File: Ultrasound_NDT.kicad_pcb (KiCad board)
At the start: 6 copper layers, 100 x 100 mm, 316 parts, among them J1 Conn_01x02_Pin, J10 CONSMA002-SMD, J11 Logger Connector, J12 UART Connector, J13 External UART, J14 External I2C, J15 JTAG Header, J16 Conn_02x04_Odd_Even, J17 Input Power, J18 Conn_01x02_Pin, J19 Conn_01x02_Pin, J2 Conn_01x02_Pin, J20 Conn_01x02_Pin, J21 Conn_01x02_Pin, J22 Conn_01x02_Pin, J23 Conn_01x02_Pin, J24 Conn_01x02_Pin, J25 Conn_01x02_Pin, J26 Spectrography Power, J27 Conn_01x02_Pin, J28 Conn_02x04_Odd_Even, J3 CONSMA002-SMD, J4 CONSMA002-SMD, J5 CONSMA002-SMD, J6 CONSMA002-SMD, J7 CONSMA002-SMD, J8 CONSMA002-SMD, J9 CONSMA002-SMD, SW1 XRSn_button, U1 AD8334ACPZ, U10 TLV9354IDR, U11 TLV9354IDR, U12 TPS63700DRCR, U13 M24M01E-FMN6TP, U14 LDL212PU50R, U15 AZ1117CH2-3.3, U16 AZ1117CH2-3.3, U17 TRS3221EIPWR, U2 DSC1001DI2-125.0000T, U3 MAX14808ETK_, U4 AD8334ACPZ, U5 F280025PNS, U6 REF3030, U7 MIC920YC5-TR, U8 TLV9354IDR, U9 TLV9354IDR, Y2 H130B-16.000-18-3030-EXT-TR

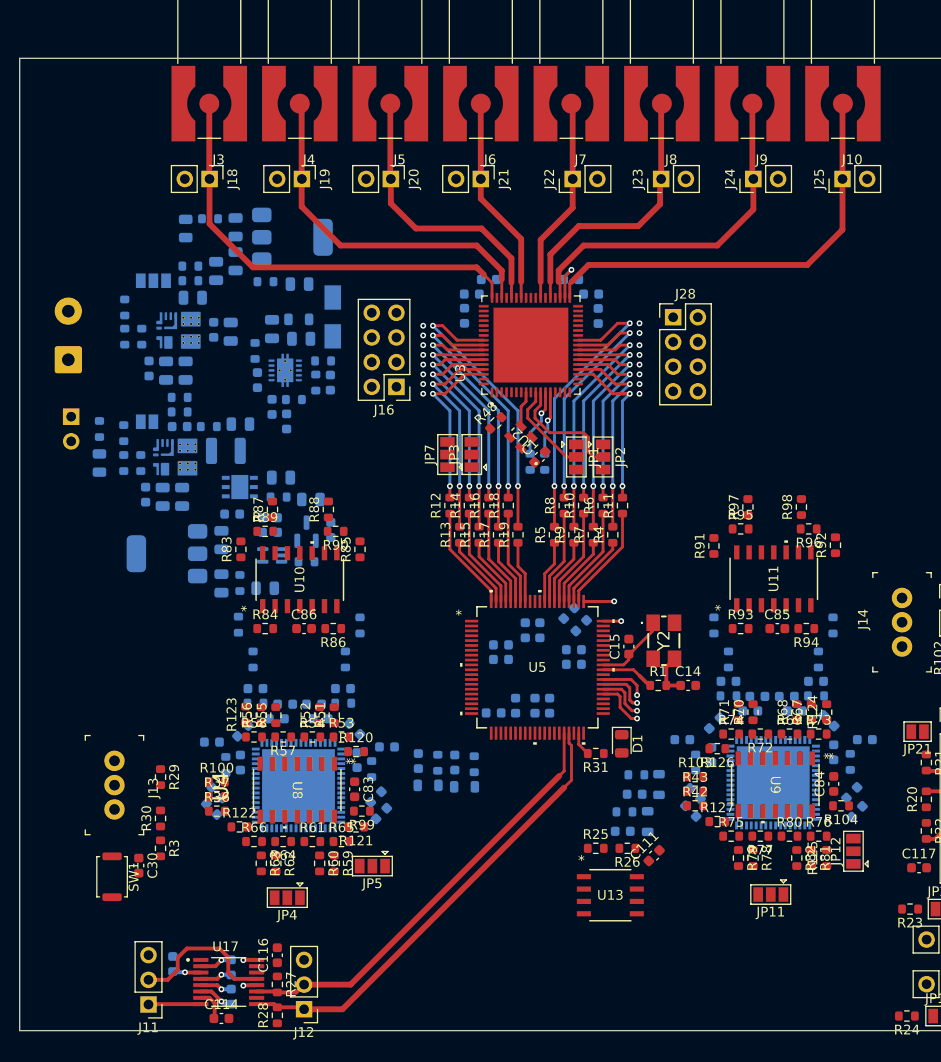
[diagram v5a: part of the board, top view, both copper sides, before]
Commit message: finished power section, 70% AFE, re-think the stackup and the AFE stage near the MCU
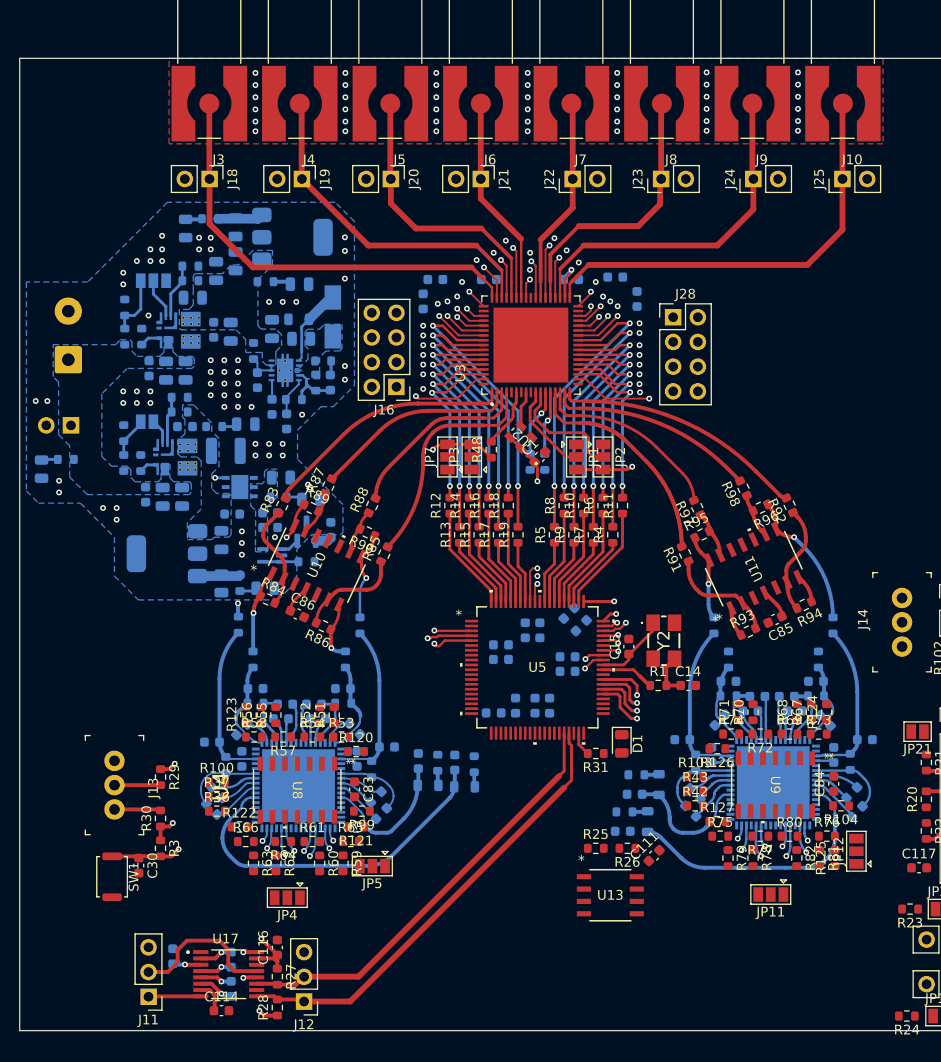
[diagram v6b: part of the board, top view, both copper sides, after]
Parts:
- moved R98 6.27 mm to (134.2, 79.0), turned to 115 degrees
- moved R92 6.25 mm to (138.9, 80.7), turned to 115 degrees
- moved R87 6.23 mm to (91.5, 78.8), turned to 65 degrees
- moved R83 6.19 mm to (86.8, 80.8), turned to 65 degrees
- moved D6 5.99 mm to (62.0, 77.0)
- moved R96 5.42 mm to (135.9, 81.0), turned to -155 degrees
- moved R89 5.32 mm to (89.8, 81.0), turned to -25 degrees
- moved R97 5.21 mm to (129.4, 81.0), turned to 115 degrees
- moved R138 4.66 mm to (64.5, 76.0), turned to 180 degrees
- moved R88 4.52 mm to (96.0, 80.8), turned to 65 degrees
- moved C7 4.50 mm to (101.2, 59.8)
- moved C5 4.37 mm to (123.2, 59.5)
- moved C12 4.04 mm to (102.5, 57.5)
- moved R95 4.00 mm to (129.9, 83.7), turned to 25 degrees
- moved R90 3.25 mm to (95.5, 83.5), turned to 155 degrees
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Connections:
- C35 pad 1: /Receiving Section/TR_OUT4 -> /Receiving Section/TR_OUT2
- C57 pad 1: /Receiving Section/TR_OUT8 -> /Receiving Section/TR_OUT6
- R128 pad 2: /Receiving Section/TR_OUT8 -> /Receiving Section/TR_OUT6
- R130 pad 2: /Receiving Section/TR_OUT4 -> /Receiving Section/TR_OUT2
- R35 pad 1: /Receiving Section/TR_OUT4 -> /Receiving Section/TR_OUT2
- R47 pad 1: /Receiving Section/TR_OUT8 -> /Receiving Section/TR_OUT6
- U1 pad 62: /Receiving Section/TR_OUT8 -> /Receiving Section/TR_OUT6
- U4 pad 62: /Receiving Section/TR_OUT4 -> /Receiving Section/TR_OUT2
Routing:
- net /Main MCU Section/RS232_FOFF: track 1.38 -> 61.8 mm, vias 1 -> 2
- net /Main MCU Section/SCIA_RX: track 0.00 -> 48.9 mm, vias 0 -> 1
- net /Main MCU Section/SCIA_TX: track 0.00 -> 48.1 mm, vias 0 -> 1
- net /Main MCU Section/XRSn: track 0.00 -> 46.5 mm, vias 0 -> 2
- net /Receiving Section/GAIN12_A: track 0.00 -> 36.6 mm
- net +3.3V_PULSE: track 0.00 -> 33.2 mm, vias 0 -> 4
- net MCU_IO_3V3: track 0.00 -> 31.3 mm, vias 0 -> 7
- net /Receiving Section/GAIN34_B: track 0.00 -> 27.9 mm
- net /Receiving Section/TR_OUT2: track 0.00 -> 26.2 mm
- net /Pulsing Section/TR1: track 0.00 -> 26.0 mm
- net /Pulsing Section/TR8: track 0.00 -> 26.0 mm
- net /Receiving Section/TR_OUT6: track 0.00 -> 25.7 mm
- net /Pulsing Section/TR4: track 0.00 -> 23.6 mm
- net /Pulsing Section/TR5: track 0.00 -> 23.1 mm
- net /Pulsing Section/TR7: track 0.00 -> 21.5 mm
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- added copper zone on B.Cu, net +12V
- added copper zone on B.Cu, net +5V
- added copper zone on B.Cu, net +5V_PULSE
- added copper zone on B.Cu, net +7V
- added copper zone on B.Cu, net -5V_PULSE
- added copper zone on B.Cu, net GND
- added copper zone on F.Cu, net GND
